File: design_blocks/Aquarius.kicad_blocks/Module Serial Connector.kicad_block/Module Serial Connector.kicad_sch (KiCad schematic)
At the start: 1 part

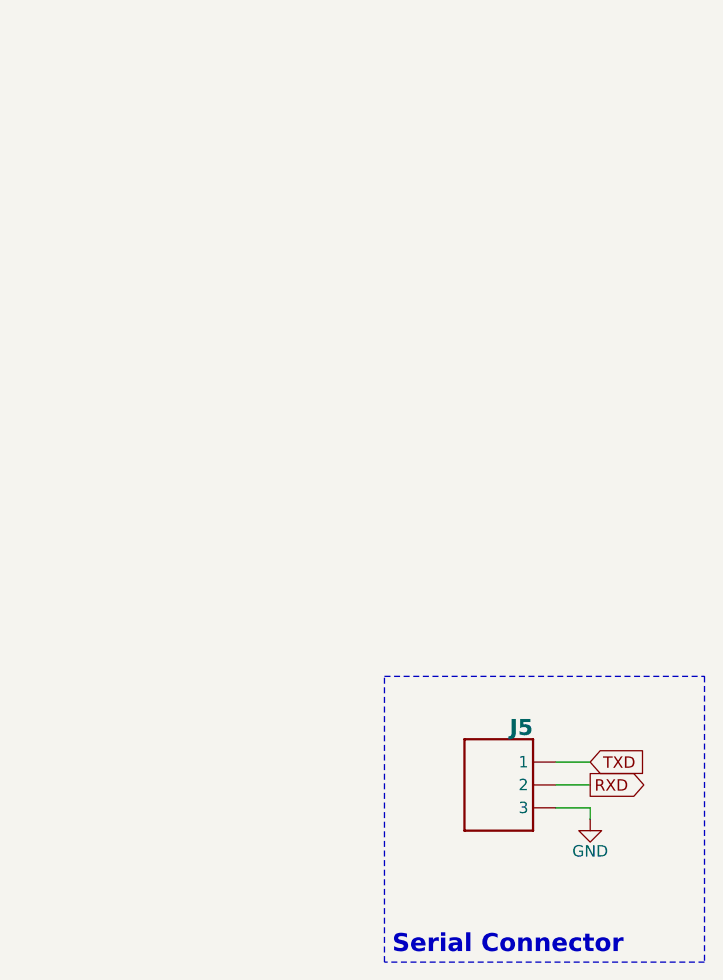
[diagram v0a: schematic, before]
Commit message: Updated blocks
Added current sensor
Updated LEDs
Updated QWICC
Changed MCU
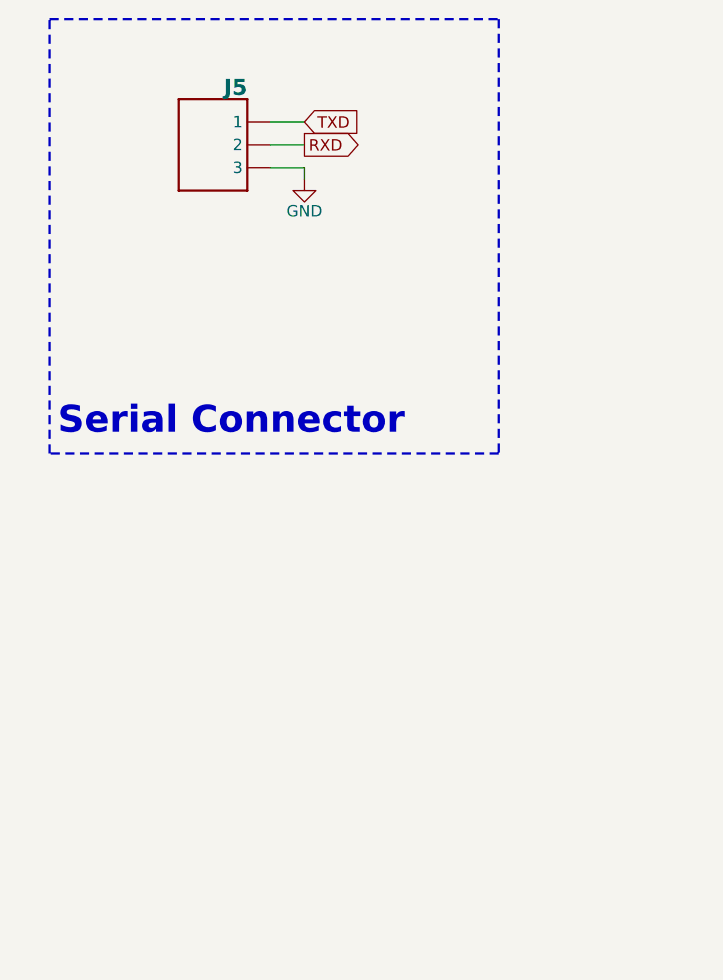
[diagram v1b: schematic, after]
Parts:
- J5: footprint Connector_JST:JST_SH_BM03B-SRSS-TB_1x03-1MP_P1.00mm_Vertical -> CRGM Connector:JST_SH_BM03B-SRSS-TB_1x03-1MP_P1.00mm_Vertical; Digikey (none) -> 455-BM04B-SRSS-TBTR-ND; LCSC C2919600 -> C2919601; MPN BM03B-SRSS-TB -> BM04B-SRSS-TB; Mouser (none) -> 306-BM04BSRSSTBTLFSN
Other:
- moved on the sheet: J5
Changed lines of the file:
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@@
 	(paper "A4")
 	(rectangle
-		(start 215.9 92.075)
-		(end 251.46 123.825)
-		(stroke
-			(width 0)
+		(start 178.69 19.05)
+		(end 228.6 67.31)
+		(stroke
+			(width 0.254)
 			(type dash)
 			(color 255 153 0 1)
@@
 	(text "Serial Connector"
 		(exclude_from_sim no)
-		(at 229.616 121.92 0)
+		(at 198.882 63.754 0)
 		(effects
 			(font
-				(size 2 2)
-				(thickness 0.4)
+				(size 3 3)
+				(thickness 0.6)
 				(bold yes)
 			)
@@
 	(wire
 		(pts
-			(xy 234.95 101.6) (xy 238.76 101.6)
-		)
-		(stroke
-			(width 0)
-			(type default)
-		)
-	)
-	(wire
-		(pts
-			(xy 238.76 107.95) (xy 238.76 106.68)
-		)
-		(stroke
-			(width 0)
-			(type default)
-		)
-	)
-	(wire
-		(pts
-			(xy 234.95 104.14) (xy 238.76 104.14)
-		)
-		(stroke
-			(width 0)
-			(type default)
-		)
-	)
-	(wire
-		(pts
-			(xy 238.76 106.68) (xy 234.95 106.68)
-		)
-		(stroke
-			(width 0)
-			(type default)
-		)
-	)
-	(global_label "RXD"
-		(shape output)
-		(at 238.76 104.14 0)
+			(xy 203.2 30.48) (xy 207.01 30.48)
+		)
+		(stroke
+			(width 0)
+			(type default)
+		)
+	)
+	(wire
+		(pts
+			(xy 207.01 36.83) (xy 207.01 35.56)
+		)
+		(stroke
+			(width 0)
+			(type default)
+		)
+	)
+	(wire
+		(pts
+			(xy 203.2 33.02) (xy 207.01 33.02)
+		)
+		(stroke
+			(width 0)
+			(type default)
+		)
+	)
+	(wire
+		(pts
+			(xy 207.01 35.56) (xy 203.2 35.56)
+		)
+		(stroke
+			(width 0)
+			(type default)
+		)
+	)
+	(global_label "TXD"
+		(shape input)
+		(at 207.01 30.48 0)
 		(fields_autoplaced yes)
 		(effects
@@
 		)
 		(property "Intersheetrefs" "${INTERSHEET_REFS}"
-			(at 245.4947 104.14 0)
+			(at 213.4423 30.48 0)
 			(effects
 				(font
@@
 		)
 	)
-	(global_label "TXD"
-		(shape input)
-		(at 238.76 101.6 0)
+	(global_label "RXD"
+		(shape output)
+		(at 207.01 33.02 0)
 		(fields_autoplaced yes)
 		(effects
@@
 		)
 		(property "Intersheetrefs" "${INTERSHEET_REFS}"
-			(at 245.1923 101.6 0)
+			(at 213.7447 33.02 0)
 			(effects
 				(font
@@
 	(symbol
 		(lib_id "power:GND")
-		(at 238.76 107.95 0)
+		(at 207.01 36.83 0)
 		(unit 1)
 		(exclude_from_sim no)
@@
 		(dnp no)
 		(property "Reference" "#PWR023"
-			(at 238.76 114.3 0)
+			(at 207.01 43.18 0)
 			(effects
 				(font
@@
 		)
 		(property "Value" "GND"
-			(at 238.76 111.506 0)
+			(at 207.01 40.386 0)
 			(effects
 				(font
@@
 		)
 		(property "Footprint" ""
-			(at 238.76 107.95 0)
+			(at 207.01 36.83 0)
 			(effects
 				(font
@@
 		)
 		(property "Datasheet" ""
-			(at 238.76 107.95 0)
+			(at 207.01 36.83 0)
 			(effects
 				(font
@@
 		)
 		(property "Description" "Power symbol creates a global label with name \"GND\" , ground"
-			(at 238.76 107.95 0)
+			(at 207.01 36.83 0)
 			(effects
 				(font
@@
 		(instances
 			(project "relay-module"
-				(path "/445c1fff-2e1a-48b1-a91f-a137832edebf"
+				(path "/445c1fff-2e1a-48b1-a91f-a137832edebf/8c24c56f-0d3c-42c7-983e-10b8f8d78981"
 					(reference "#PWR023")
 					(unit 1)
@@
 	(symbol
 		(lib_id "CRGM Connector:JST-SH-3")
-		(at 232.41 101.6 0)
+		(at 200.66 30.48 0)
 		(mirror y)
 		(unit 1)
@@
 		(dnp no)
 		(property "Reference" "J5"
-			(at 232.41 98.806 0)
+			(at 200.66 27.686 0)
 			(effects
 				(font
@@
 		)
 		(property "Value" "~"
-			(at 232.41 112.014 0)
+			(at 200.66 40.894 0)
 			(effects
 				(font
@@
 				)
 				(justify left top)
-			)
-		)
-		(property "Footprint" "Connector_JST:JST_SH_BM03B-SRSS-TB_1x03-1MP_P1.00mm_Vertical"
-			(at 231.14 92.71 0)
-			(effects
-				(font
-					(size 1.27 1.27)
-				)
-				(hide yes)
-			)
-		)
-		(property "Datasheet" ""
-			(at 232.41 101.6 0)
+				(hide yes)
+			)
+		)
+		(property "Footprint" "CRGM Connector:JST_SH_BM03B-SRSS-TB_1x03-1MP_P1.00mm_Vertical"
+			(at 199.39 21.59 0)
+			(effects
+				(font
+					(size 1.27 1.27)
+				)
+				(hide yes)
+			)
+		)
+		(property "Datasheet" "https://www.jst-mfg.com/product/pdf/eng/eSH.pdf"
+			(at 200.66 30.48 0)
 			(effects
 				(font
@@
 		)
 		(property "Description" "JST SH 1.0mm 3 Position"
-			(at 230.378 95.25 0)
+			(at 198.628 24.13 0)
 			(effects
 				(font
@@
 		)
 		(property "MN" "JST"
-			(at 232.41 101.6 0)
-			(effects
-				(font
-					(size 1.27 1.27)
-				)
-				(hide yes)
-			)
-		)
-		(property "MPN" "BM03B-SRSS-TB"
-			(at 232.41 101.6 0)
-			(effects
-				(font
-					(size 1.27 1.27)
-				)
-				(hide yes)
-			)
-		)
-		(property "Digikey" ""
-			(at 232.41 101.6 0)
-			(effects
-				(font
-					(size 1.27 1.27)
-				)
-				(hide yes)
-			)
-		)
-		(property "Mouser" ""
-			(at 232.41 101.6 0)
-			(effects
-				(font
-					(size 1.27 1.27)
-				)
-				(hide yes)
-			)
-		)
-		(property "LCSC" "C2919600"
-			(at 232.41 101.6 0)
+			(at 200.66 30.48 0)
+			(effects
+				(font
+					(size 1.27 1.27)
+				)
+				(hide yes)
+			)
+		)
+		(property "MPN" "BM04B-SRSS-TB"
+			(at 200.66 30.48 0)
+			(effects
+				(font
+					(size 1.27 1.27)
+				)
+				(hide yes)
+			)
+		)
+		(property "Digikey" "455-BM04B-SRSS-TBTR-ND"
+			(at 200.66 30.48 0)
+			(effects
+				(font
+					(size 1.27 1.27)
+				)
+				(hide yes)
+			)
+		)
+		(property "Mouser" "306-BM04BSRSSTBTLFSN"
+			(at 200.66 30.48 0)
+			(effects
+				(font
+					(size 1.27 1.27)
+				)
+				(hide yes)
+			)
+		)
+		(property "LCSC" "C2919601"
+			(at 200.66 30.48 0)
 			(effects
 				(font
@@
 		)
 		(instances
-			(project ""
-				(path "/445c1fff-2e1a-48b1-a91f-a137832edebf"
+			(project "relay-module"
+				(path "/445c1fff-2e1a-48b1-a91f-a137832edebf/8c24c56f-0d3c-42c7-983e-10b8f8d78981"
 					(reference "J5")
 					(unit 1)
